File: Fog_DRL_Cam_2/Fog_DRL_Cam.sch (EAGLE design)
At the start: 52 parts, among them IC1 78L05Z, K1 CQ1-12V, K2 CQ1-12V, Q1 IRLML2502, Q2 16MHz, U1 ATTINY24A-SU, X1 RCAX2, X10 PROG-ISP6POGOPIN, X2 PS/2, X3 JST2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

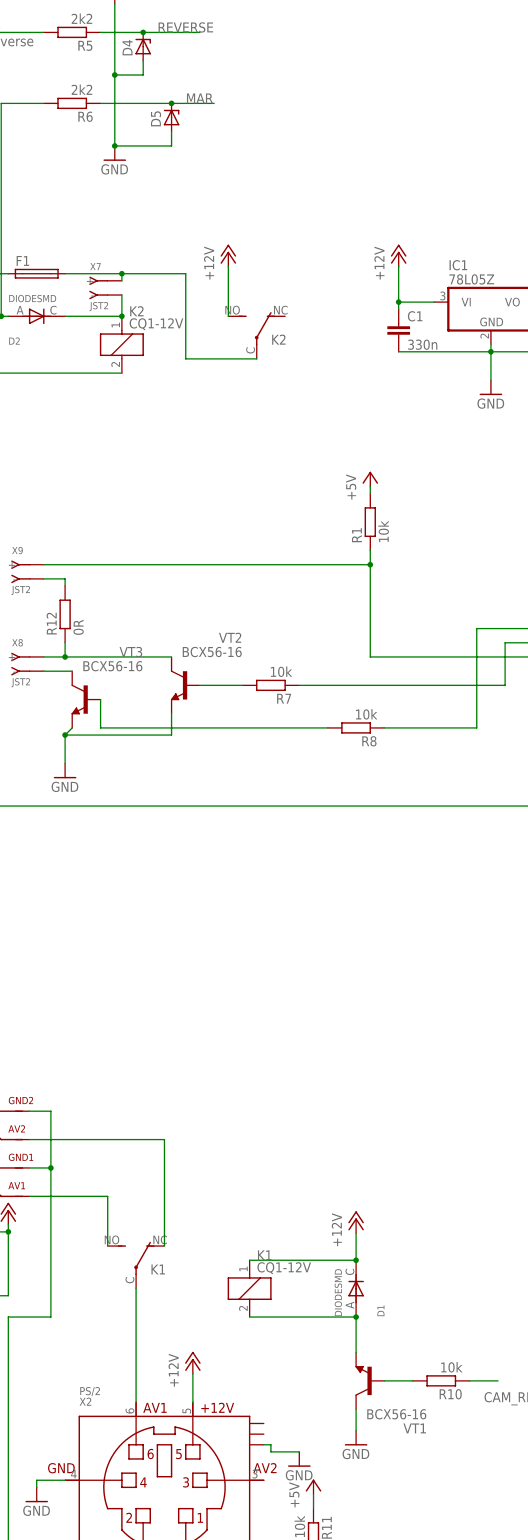
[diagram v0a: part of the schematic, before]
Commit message: Добавлены ДХО работающие на ШИМ
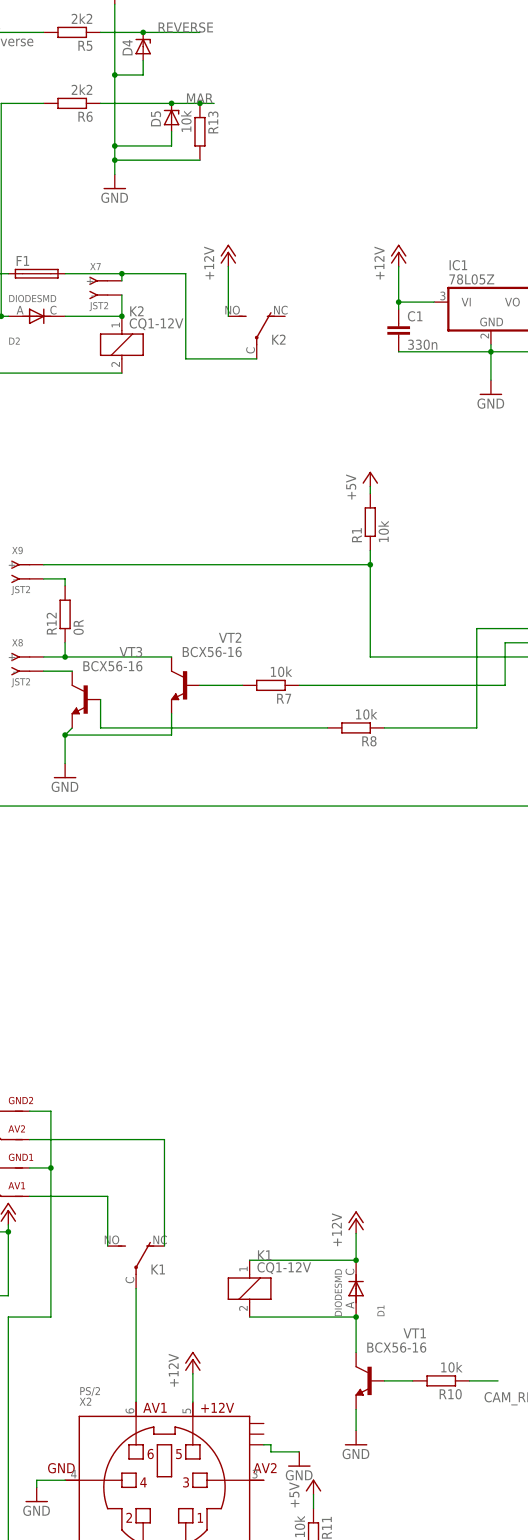
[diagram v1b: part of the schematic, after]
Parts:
- added R13: 10k, rcl:R-EU_R0603
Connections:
- net GND: now also R13.2, VT1.E; no longer VT1.C
- net MAR: now also R13.1
- net N$5: now also VT1.C; no longer VT1.E
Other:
- moved on the sheet: VT1
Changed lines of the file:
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@@
 <part name="R6" library="rcl" deviceset="R-EU_" device="R0603" value="2k2"/>
 <part name="D5" library="diode" deviceset="ZENER-DIODE" device="SOD80C"/>
+<part name="R13" library="rcl" deviceset="R-EU_" device="R0603" value="10k"/>
 </parts>
 <sheets>
@@
 <instance part="X1" gate="G$1" x="-157.48" y="17.78"/>
 <instance part="X2" gate="G$1" x="-140.97" y="-46.99"/>
-<instance part="VT1" gate="G$1" x="-88.9" y="-15.24" rot="R180"/>
+<instance part="VT1" gate="G$1" x="-88.9" y="-15.24" rot="MR0"/>
 <instance part="VT2" gate="G$1" x="-121.92" y="109.22" rot="MR0"/>
 <instance part="VT3" gate="G$1" x="-139.7" y="106.68" rot="MR0"/>
@@
 <instance part="R4" gate="G$1" x="-142.24" y="236.22" rot="R180"/>
 <instance part="R5" gate="G$1" x="-142.24" y="226.06" rot="R180"/>
-<instance part="GND11" gate="1" x="-134.62" y="203.2"/>
+<instance part="GND11" gate="1" x="-134.62" y="198.12"/>
 <instance part="GND12" gate="1" x="81.28" y="96.52"/>
 <instance part="P+10" gate="1" x="73.66" y="180.34"/>
@@
 <instance part="R6" gate="G$1" x="-142.24" y="213.36" rot="R180"/>
 <instance part="D5" gate="G$1" x="-124.46" y="210.82" rot="R90"/>
+<instance part="R13" gate="G$1" x="-119.38" y="208.28" rot="R270"/>
 </instances>
 <busses>
@@
 <pinref part="K1" gate="1" pin="2"/>
 <wire x1="-91.44" y1="-3.81" x2="-110.49" y2="-3.81" width="0.1524" layer="91"/>
-<pinref part="VT1" gate="G$1" pin="E"/>
+<pinref part="VT1" gate="G$1" pin="C"/>
 <wire x1="-91.44" y1="-10.16" x2="-91.44" y2="-3.81" width="0.1524" layer="91"/>
 <junction x="-91.44" y="-3.81"/>
@@
 <net name="GND" class="0">
 <segment>
-<pinref part="GND4" gate="1" pin="GND"/>
-<pinref part="VT1" gate="G$1" pin="C"/>
-<wire x1="-91.44" y1="-24.13" x2="-91.44" y2="-20.32" width="0.1524" layer="91"/>
-</segment>
-<segment>
 <pinref part="X2" gate="G$1" pin="4"/>
 <pinref part="GND6" gate="1" pin="GND"/>
@@
 <wire x1="-134.62" y1="231.14" x2="-134.62" y2="218.44" width="0.1524" layer="91"/>
 <wire x1="-134.62" y1="218.44" x2="-134.62" y2="205.74" width="0.1524" layer="91"/>
+<wire x1="-134.62" y1="205.74" x2="-134.62" y2="203.2" width="0.1524" layer="91"/>
+<wire x1="-134.62" y1="203.2" x2="-134.62" y2="200.66" width="0.1524" layer="91"/>
 <wire x1="-129.54" y1="220.98" x2="-129.54" y2="218.44" width="0.1524" layer="91"/>
 <wire x1="-129.54" y1="218.44" x2="-134.62" y2="218.44" width="0.1524" layer="91"/>
@@
 <wire x1="-124.46" y1="205.74" x2="-134.62" y2="205.74" width="0.1524" layer="91"/>
 <junction x="-134.62" y="205.74"/>
+<pinref part="R13" gate="G$1" pin="2"/>
+<wire x1="-119.38" y1="203.2" x2="-134.62" y2="203.2" width="0.1524" layer="91"/>
+<junction x="-134.62" y="203.2"/>
 </segment>
 <segment>
@@
 <wire x1="60.96" y1="101.6" x2="81.28" y2="101.6" width="0.1524" layer="91"/>
 <junction x="81.28" y="101.6"/>
+</segment>
+<segment>
+<pinref part="GND4" gate="1" pin="GND"/>
+<pinref part="VT1" gate="G$1" pin="E"/>
+<wire x1="-91.44" y1="-24.13" x2="-91.44" y2="-20.32" width="0.1524" layer="91"/>
 </segment>
 </net>
@@
 <pinref part="D5" gate="G$1" pin="C"/>
 <wire x1="-137.16" y1="213.36" x2="-124.46" y2="213.36" width="0.1524" layer="91"/>
-<wire x1="-124.46" y1="213.36" x2="-116.84" y2="213.36" width="0.1524" layer="91"/>
+<wire x1="-124.46" y1="213.36" x2="-119.38" y2="213.36" width="0.1524" layer="91"/>
 <junction x="-124.46" y="213.36"/>
 <label x="-121.92" y="213.36" size="1.778" layer="95"/>
-</segment>
-<segment>
+<pinref part="R13" gate="G$1" pin="1"/>
+<wire x1="-119.38" y1="213.36" x2="-116.84" y2="213.36" width="0.1524" layer="91"/>
+<junction x="-119.38" y="213.36"/>
+</segment>
+<segment>
